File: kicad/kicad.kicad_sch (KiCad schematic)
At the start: 29 parts, among them J101 DEBUG_LED_CONN, J102 EPD_SPI_CONN, J103 HPC_CONN, J104 STORAGE_CONN, J105 USBC_CONN, J106 GLOBAL_CONN, J107 INPUT_CONN, J108 CHARGER_CONN

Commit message: refactor usb-c module, remove unnecessary ICs
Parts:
- removed J105: USBC_CONN, Connector_JST:JST_XH_B3B-XH-A_1x03_P2.50mm_Vertical, symbol Connector_Generic:Conn_01x03
- removed JP104: USB_PWR_JP, Jumper:SolderJumper-2_P1.3mm_Open_TrianglePad1.0x1.5mm, symbol Jumper:SolderJumper_2_Open
- added J109: USBC_CONN, Connector_JST:JST_XH_B2B-XH-A_1x02_P2.50mm_Vertical, symbol Connector_Generic:Conn_01x02
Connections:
- net USB-C/DM: now also J109.1 (Pin_1)
- net USB-C/DP: now also J109.2 (Pin_2)
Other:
- sheet USB-C ports: added none; removed FLT_N, IC_PWR
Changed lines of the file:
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@@
 	(wire
 		(pts
-			(xy 153.67 49.53) (xy 147.32 49.53)
-		)
-		(stroke
-			(width 0)
-			(type default)
-		)
-	)
-	(wire
-		(pts
 			(xy 261.62 72.39) (xy 261.62 49.53)
 		)
@@
 	(wire
 		(pts
-			(xy 153.67 60.96) (xy 153.67 49.53)
-		)
-		(stroke
-			(width 0)
-			(type default)
-		)
-	)
-	(wire
-		(pts
 			(xy 38.1 143.51) (xy 39.37 143.51)
 		)
@@
 		)
 	)
-	(text "DEFAULT \nCONNECTED"
-		(exclude_from_sim no)
-		(at 102.362 38.354 0)
-		(effects
-			(font
-				(size 1.27 1.27)
-			)
-		)
-	)
 	(symbol
 		(lib_id "Device:R")
@@
 	)
 	(symbol
-		(lib_id "Connector_Generic:Conn_01x03")
-		(at 158.75 63.5 0)
-		(unit 1)
-		(exclude_from_sim no)
-		(in_bom yes)
-		(on_board yes)
-		(dnp no)
-		(fields_autoplaced yes)
-		(property "Reference" "J105"
-			(at 161.29 62.2299 0)
-			(effects
-				(font
-					(size 1.27 1.27)
-				)
-				(justify left)
-			)
-		)
-		(property "Value" "USBC_CONN"
-			(at 161.29 64.7699 0)
-			(effects
-				(font
-					(size 1.27 1.27)
-				)
-				(justify left)
-			)
-		)
-		(property "Footprint" "Connector_JST:JST_XH_B3B-XH-A_1x03_P2.50mm_Vertical"
-			(at 158.75 63.5 0)
-			(effects
-				(font
-					(size 1.27 1.27)
-				)
-				(hide yes)
-			)
-		)
-		(property "Datasheet" "~"
-			(at 158.75 63.5 0)
-			(effects
-				(font
-					(size 1.27 1.27)
-				)
-				(hide yes)
-			)
-		)
-		(property "Description" "Generic connector, single row, 01x03, script generated (kicad-library-utils/schlib/autogen/connector/)"
-			(at 158.75 63.5 0)
-			(effects
-				(font
-					(size 1.27 1.27)
-				)
-				(hide yes)
-			)
-		)
-		(pin "1"
-		)
-		(pin "3"
-		)
-		(pin "2"
-		)
-		(instances
-			(project "kicad"
-				(path "/97e37379-fec6-4f0d-82d9-4ea53516bb02"
-					(reference "J105")
-					(unit 1)
-				)
-			)
-		)
-	)
-	(symbol
 		(lib_id "Device:R")
 		(at 31.75 104.14 0)
@@
 	)
 	(symbol
-		(lib_id "power:+3.3V")
-		(at 111.76 45.72 0)
+		(lib_id "power:GND")
+		(at 39.37 158.75 0)
 		(unit 1)
 		(exclude_from_sim no)
@@
 		(dnp no)
 		(fields_autoplaced yes)
-		(property "Reference" "#PWR0113"
-			(at 111.76 49.53 0)
+		(property "Reference" "#PWR0103"
+			(at 39.37 165.1 0)
 			(effects
 				(font
@@
 			)
 		)
-		(property "Value" "+3.3V"
-			(at 111.76 40.64 0)
+		(property "Value" "GND"
+			(at 39.37 163.83 0)
 			(effects
 				(font
 					(size 1.27 1.27)
 				)
+				(hide yes)
 			)
 		)
 		(property "Footprint" ""
-			(at 111.76 45.72 0)
+			(at 39.37 158.75 0)
 			(effects
 				(font
@@
 		)
 		(property "Datasheet" ""
-			(at 111.76 45.72 0)
+			(at 39.37 158.75 0)
 			(effects
 				(font
@@
 			)
 		)
-		(property "Description" "Power symbol creates a global label with name \"+3.3V\""
-			(at 111.76 45.72 0)
+		(property "Description" "Power symbol creates a global label with name \"GND\" , ground"
+			(at 39.37 158.75 0)
 			(effects
 				(font
@@
 			(project "kicad"
 				(path "/97e37379-fec6-4f0d-82d9-4ea53516bb02"
-					(reference "#PWR0113")
+					(reference "#PWR0103")
 					(unit 1)
 				)
@@
 	)
 	(symbol
-		(lib_id "power:GND")
-		(at 39.37 158.75 0)
+		(lib_id "Connector_Generic:Conn_01x03")
+		(at 33.02 140.97 180)
 		(unit 1)
 		(exclude_from_sim no)
@@
 		(dnp no)
 		(fields_autoplaced yes)
-		(property "Reference" "#PWR0103"
-			(at 39.37 165.1 0)
+		(property "Reference" "J101"
+			(at 33.02 132.08 0)
 			(effects
 				(font
 					(size 1.27 1.27)
 				)
-				(hide yes)
 			)
 		)
-		(property "Value" "GND"
-			(at 39.37 163.83 0)
+		(property "Value" "DEBUG_LED_CONN"
+			(at 33.02 134.62 0)
 			(effects
 				(font
 					(size 1.27 1.27)
 				)
-				(hide yes)
 			)
 		)
-		(property "Footprint" ""
-			(at 39.37 158.75 0)
+		(property "Footprint" "Connector_JST:JST_XH_B3B-XH-A_1x03_P2.50mm_Vertical"
+			(at 33.02 140.97 0)
 			(effects
 				(font
@@
 			)
 		)
-		(property "Datasheet" ""
-			(at 39.37 158.75 0)
+		(property "Datasheet" "~"
+			(at 33.02 140.97 0)
 			(effects
 				(font
@@
 			)
 		)
-		(property "Description" "Power symbol creates a global label with name \"GND\" , ground"
-			(at 39.37 158.75 0)
+		(property "Description" "Generic connector, single row, 01x03, script generated (kicad-library-utils/schlib/autogen/connector/)"
+			(at 33.02 140.97 0)
 			(effects
 				(font
@@
 		(pin "1"
 		)
+		(pin "3"
+		)
+		(pin "2"
+		)
 		(instances
 			(project "kicad"
 				(path "/97e37379-fec6-4f0d-82d9-4ea53516bb02"
-					(reference "#PWR0103")
+					(reference "J101")
 					(unit 1)
 				)
@@
 	)
 	(symbol
-		(lib_id "Connector_Generic:Conn_01x03")
-		(at 33.02 140.97 180)
+		(lib_id "Connector_Generic:Conn_01x02")
+		(at 158.75 63.5 0)
 		(unit 1)
 		(exclude_from_sim no)
@@
 		(on_board yes)
 		(dnp no)
-		(fields_autoplaced yes)
-		(property "Reference" "J101"
-			(at 33.02 132.08 0)
+		(property "Reference" "J109"
+			(at 159.004 69.342 0)
 			(effects
 				(font
@@
 			)
 		)
-		(property "Value" "DEBUG_LED_CONN"
-			(at 33.02 134.62 0)
+		(property "Value" "USBC_CONN"
+			(at 159.004 71.882 0)
 			(effects
 				(font
@@
 			)
 		)
-		(property "Footprint" "Connector_JST:JST_XH_B3B-XH-A_1x03_P2.50mm_Vertical"
-			(at 33.02 140.97 0)
+		(property "Footprint" "Connector_JST:JST_XH_B2B-XH-A_1x02_P2.50mm_Vertical"
+			(at 158.75 63.5 0)
 			(effects
 				(font
@@
 		)
 		(property "Datasheet" "~"
-			(at 33.02 140.97 0)
+			(at 158.75 63.5 0)
 			(effects
 				(font
@@
 			)
 		)
-		(property "Description" "Generic connector, single row, 01x03, script generated (kicad-library-utils/schlib/autogen/connector/)"
-			(at 33.02 140.97 0)
+		(property "Description" "Generic connector, single row, 01x02, script generated (kicad-library-utils/schlib/autogen/connector/)"
+			(at 158.75 63.5 0)
 			(effects
 				(font
@@
 			)
 		)
-		(pin "1"
-		)
-		(pin "3"
-		)
 		(pin "2"
 		)
+		(pin "1"
+		)
 		(instances
 			(project "kicad"
 				(path "/97e37379-fec6-4f0d-82d9-4ea53516bb02"
-					(reference "J101")
+					(reference "J109")
 					(unit 1)
 				)
@@
 	)
 	(symbol
-		(lib_id "Jumper:SolderJumper_2_Open")
-		(at 115.57 45.72 0)
-		(unit 1)
-		(exclude_from_sim yes)
-		(in_bom no)
-		(on_board yes)
-		(dnp no)
-		(property "Reference" "JP104"
-			(at 104.14 43.688 0)
-			(effects
-				(font
-					(size 1.27 1.27)
-				)
-			)
-		)
-		(property "Value" "USB_PWR_JP"
-			(at 104.14 46.228 0)
-			(effects
-				(font
-					(size 1.27 1.27)
-				)
-			)
-		)
-		(property "Footprint" "Jumper:SolderJumper-2_P1.3mm_Open_TrianglePad1.0x1.5mm"
-			(at 115.57 45.72 0)
-			(effects
-				(font
-					(size 1.27 1.27)
-				)
-				(hide yes)
-			)
-		)
-		(property "Datasheet" "~"
-			(at 115.57 45.72 0)
-			(effects
-				(font
-					(size 1.27 1.27)
-				)
-				(hide yes)
-			)
-		)
-		(property "Description" "Solder Jumper, 2-pole, open"
-			(at 115.57 45.72 0)
-			(effects
-				(font
-					(size 1.27 1.27)
-				)
-				(hide yes)
-			)
-		)
-		(pin "2"
-		)
-		(pin "1"
-		)
-		(instances
-			(project "kicad"
-				(path "/97e37379-fec6-4f0d-82d9-4ea53516bb02"
-					(reference "JP104")
-					(unit 1)
-				)
-			)
-		)
-	)
-	(symbol
 		(lib_id "power:GND")
 		(at 48.26 115.57 0)
@@
 			)
 		)
-		(pin "IC_PWR" input
-			(at 119.38 45.72 180)
-			(effects
-				(font
-					(size 1.27 1.27)
-				)
-				(justify left)
-			)
-		)
 		(pin "VBUS" output
 			(at 147.32 45.72 0)
 			(effects
 				(font
-					(size 1.27 1.27)
-				)
-				(justify right)
-			)
-		)
-		(pin "FLT_N" output
-			(at 147.32 49.53 0)
-			(effects
-				(font

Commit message: add some assembly files, but transition towards all hand
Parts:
- D101, D102, D103, D104, D105, D106, J101, J102, J103, J104, J106, J107, J108, J109, JP101, JP102, JP103, JP105, JP106, JP107, R102, R103, R104, R105, TP101, TP102: JLC (none) -> XXXXXX; LCSC (none) -> XXXXXX
- R101: JLC (none) -> 0603
- R106: value 5 -> 5.1; JLC (none) -> XXXXXX; LCSC (none) -> XXXXXX

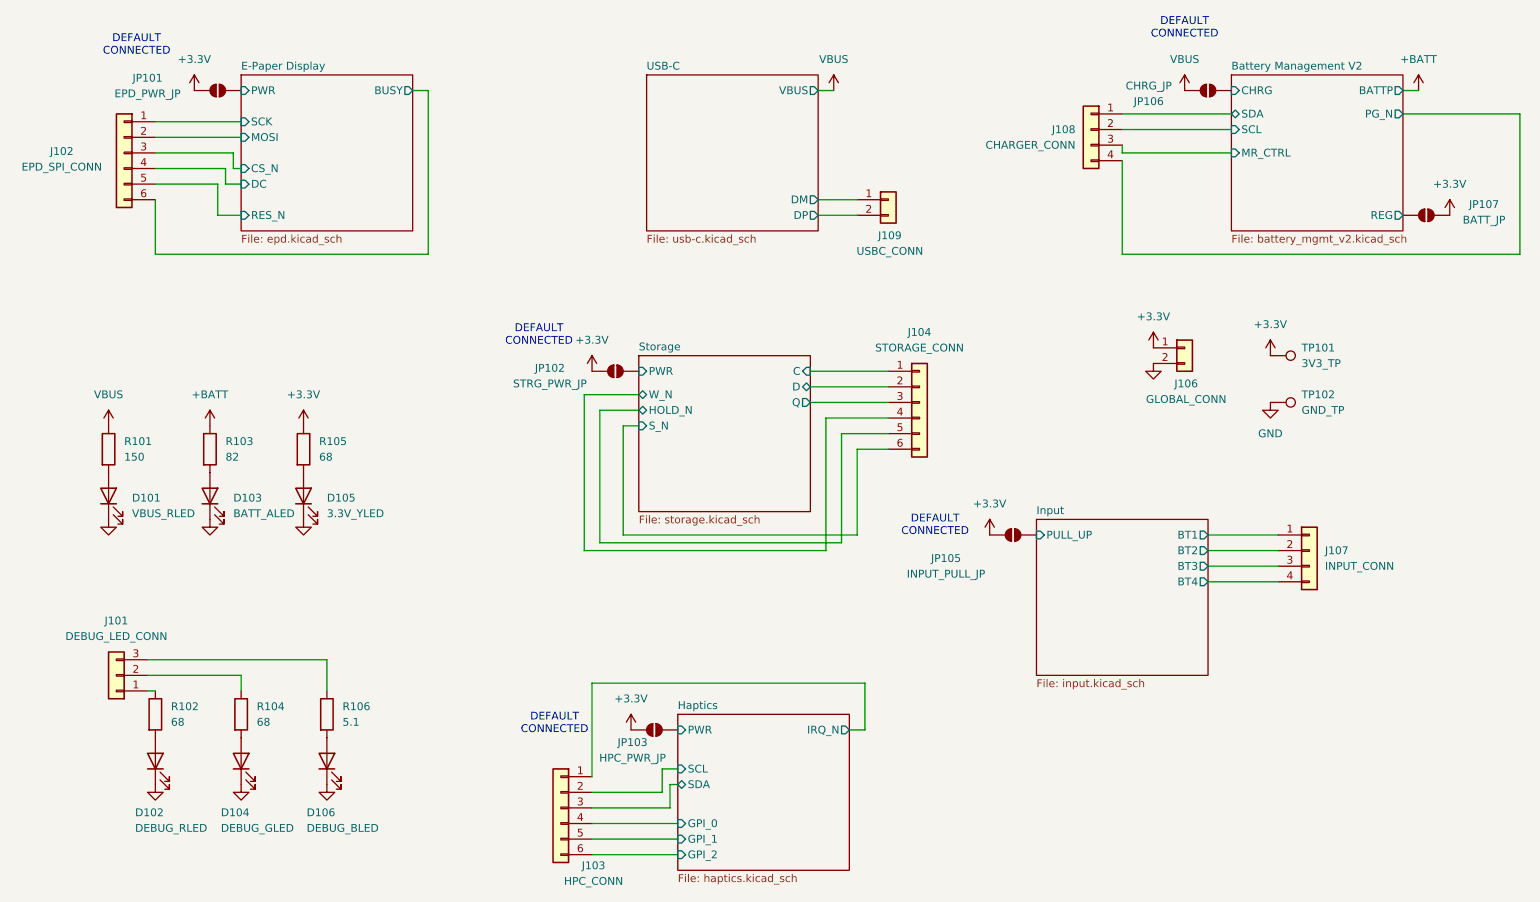
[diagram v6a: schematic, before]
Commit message: new battery management w/ separate LDO/charger almost done
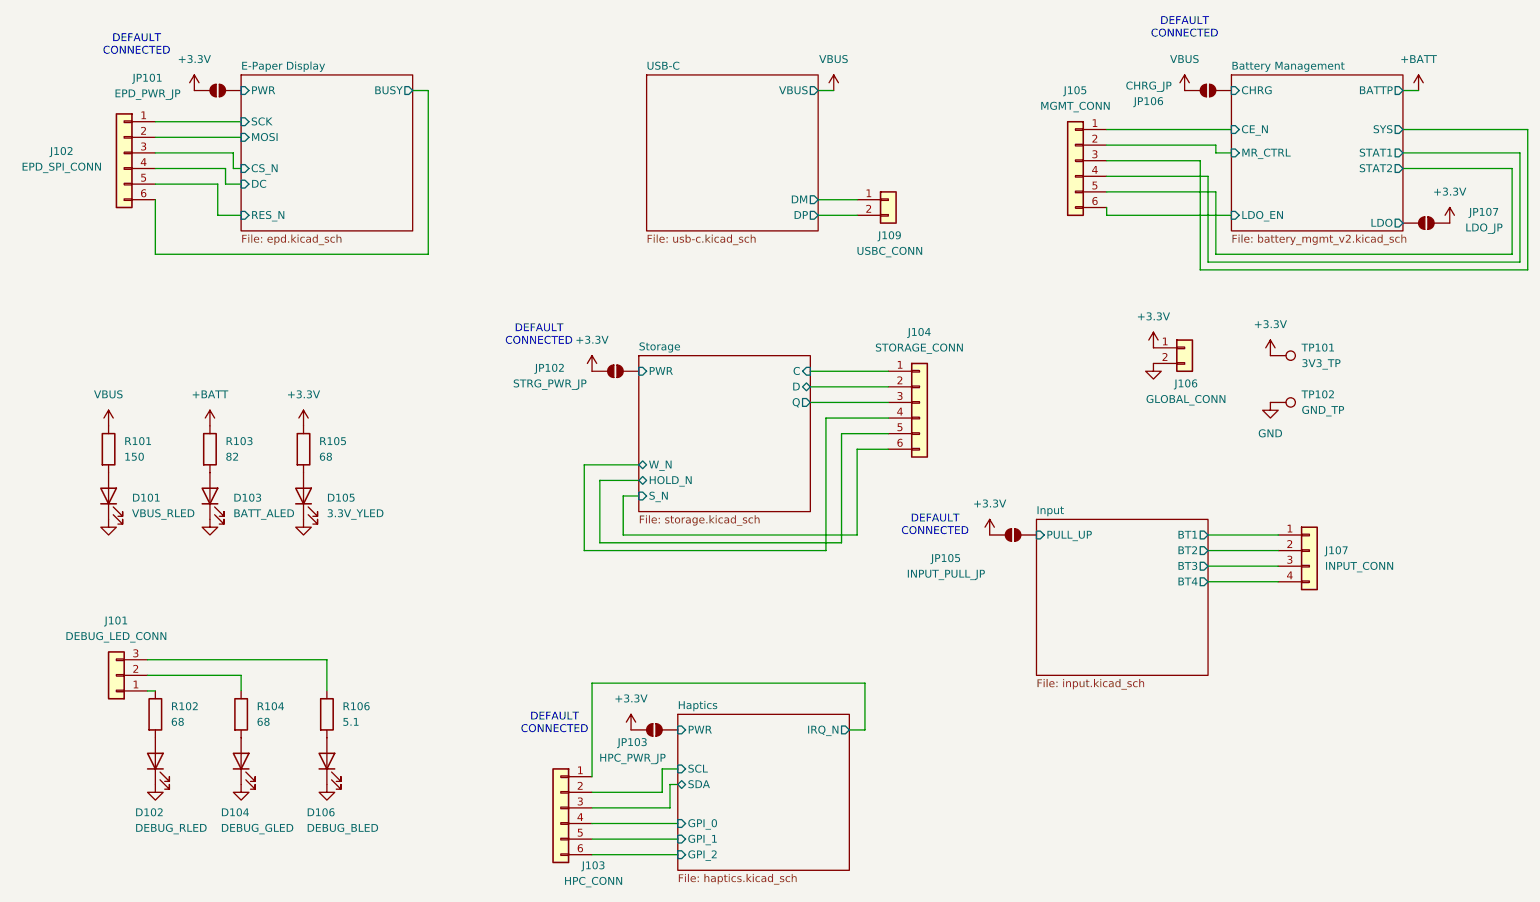
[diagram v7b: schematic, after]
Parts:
- removed J108: CHARGER_CONN, Connector_JST:JST_XH_B4B-XH-A_1x04_P2.50mm_Vertical, symbol Connector_Generic:Conn_01x04
- added J105: MGMT_CONN, Connector_JST:JST_XH_B6B-XH-A_1x06_P2.50mm_Vertical, symbol Connector_Generic:Conn_01x06
- JP107: value BATT_JP -> LDO_JP
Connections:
- net Battery Management/MR_CTRL: now also J105.2 (Pin_2)
- net Battery Management/REG renamed Battery Management/LDO
- new net Battery Management/CE_N: J105.1 (Pin_1)
- new net Battery Management/LDO_EN: J105.6 (Pin_6)
- new net Battery Management/STAT1: J105.4 (Pin_4)
- new net Battery Management/STAT2: J105.5 (Pin_5)
- new net Battery Management/SYS: J105.3 (Pin_3)
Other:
- sheet Battery Management V2 renamed Battery Management
- sheet Battery Management ports: added CE_N, LDO, LDO_EN, STAT1, STAT2, SYS; removed PG_N, REG, SCL, SDA
- company: Author: Lucas Merritt -> Mosaic Labs
- moved on the sheet: JP107
